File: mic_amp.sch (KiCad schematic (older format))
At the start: 12 parts

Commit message: * Sch edited and checked
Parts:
- removed C?: C, CAP_0603, symbol C
- removed R?: R, RES_0603, symbol R
- removed XL?: CONN_2, symbol CONN_2
- added C1: 10n, CAP_0603, symbol C
- added C2, C9: 1u, CAP_0603, symbol C
- added C6: 0.1u, CAP_0603, symbol C
- added DA1: NCP662SQ, symbol NCP662SQ
- added F1, F2, F3: Fuse0R, symbol Fuse0R
- added R1: 1M, RES_0603, symbol R
- added R5: 20k, symbol RVar
- added XL1: USB_MINI_B, symbol USB_MINI_B
- added XL2, XL3: CONN_AUDIO_SIMPLE, symbol CONN_AUDIO_SIMPLE
- R2: renamed from R?; value 2.21k -> 2k
- gave numbers to parts that had none: 8
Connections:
- net GND: now also D1.11 (NC), D1.4 (NC), C1.2, C2.2, C6.2, DA1.1 (GND), F1.2, F3.2, R1.2, R5.2, XL1.4 (UGND), XL1.5 (UID), XL2.1 (COM), XL2.H, XL3.1 (COM), XL3.H; no longer D1.9 (A/R)
- net MICBIAS: now also D1.13 (MICBIAS), R2.2, R3.1; no longer R3.2
- net VDD: now also C6.1, DA1.3 (Vout), F2.1; no longer D1.10 (GAIN)
- net at D1.14 (TH), R4.1: now also R3.2; no longer R3.1
- net at D1.6 (OUT): now also C9.1
- net MICIN: now reaches C4.2, D1.8 (MICIN)
- net at C4.1, R2.1: now also XL2.3 (L_IN)
- new net: D1.10 (GAIN), F2.2, F3.1
- new net: D1.9 (A/R), F1.1
- new net: R5.3, XL3.3 (L_IN)
- new net: C9.2, R5.1
- new net: C2.1, DA1.2 (Vin), DA1.4 (EN), XL1.1 (UVcc)
- new net: C1.1, R1.1, XL1.SHLD
- no-connect marks 0 -> 4
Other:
- note added: "Attack/release ratio:\nSoldered: 1:500\nNot soldered: 1:4000"
- note added: "Connect TH to MICBIAS\nto disable the AGC."
- note added: "Gain select:\nGAIN = Vdd: gain = 40dB\nGAIN = GND: gain = 50dB\nGAIN not connected: gain = 60dB"
- moved on the sheet: C4, R2, R3, R4

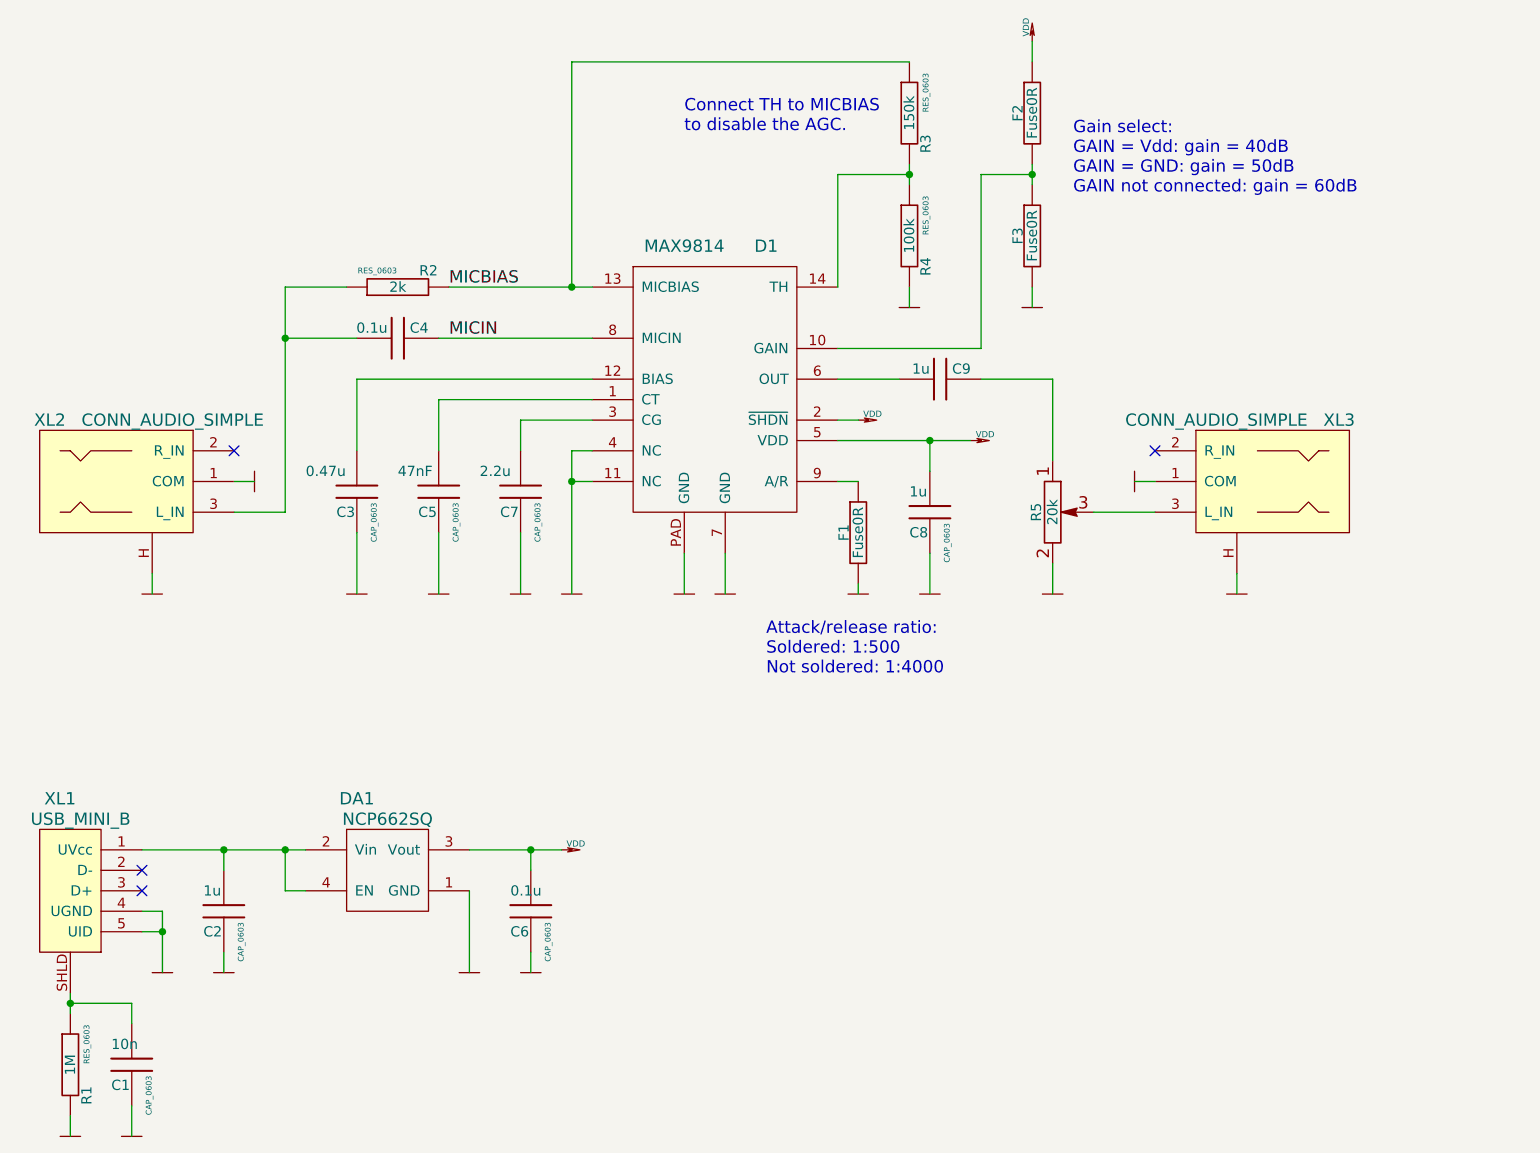
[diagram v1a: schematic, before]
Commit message: * Sch done + Components association
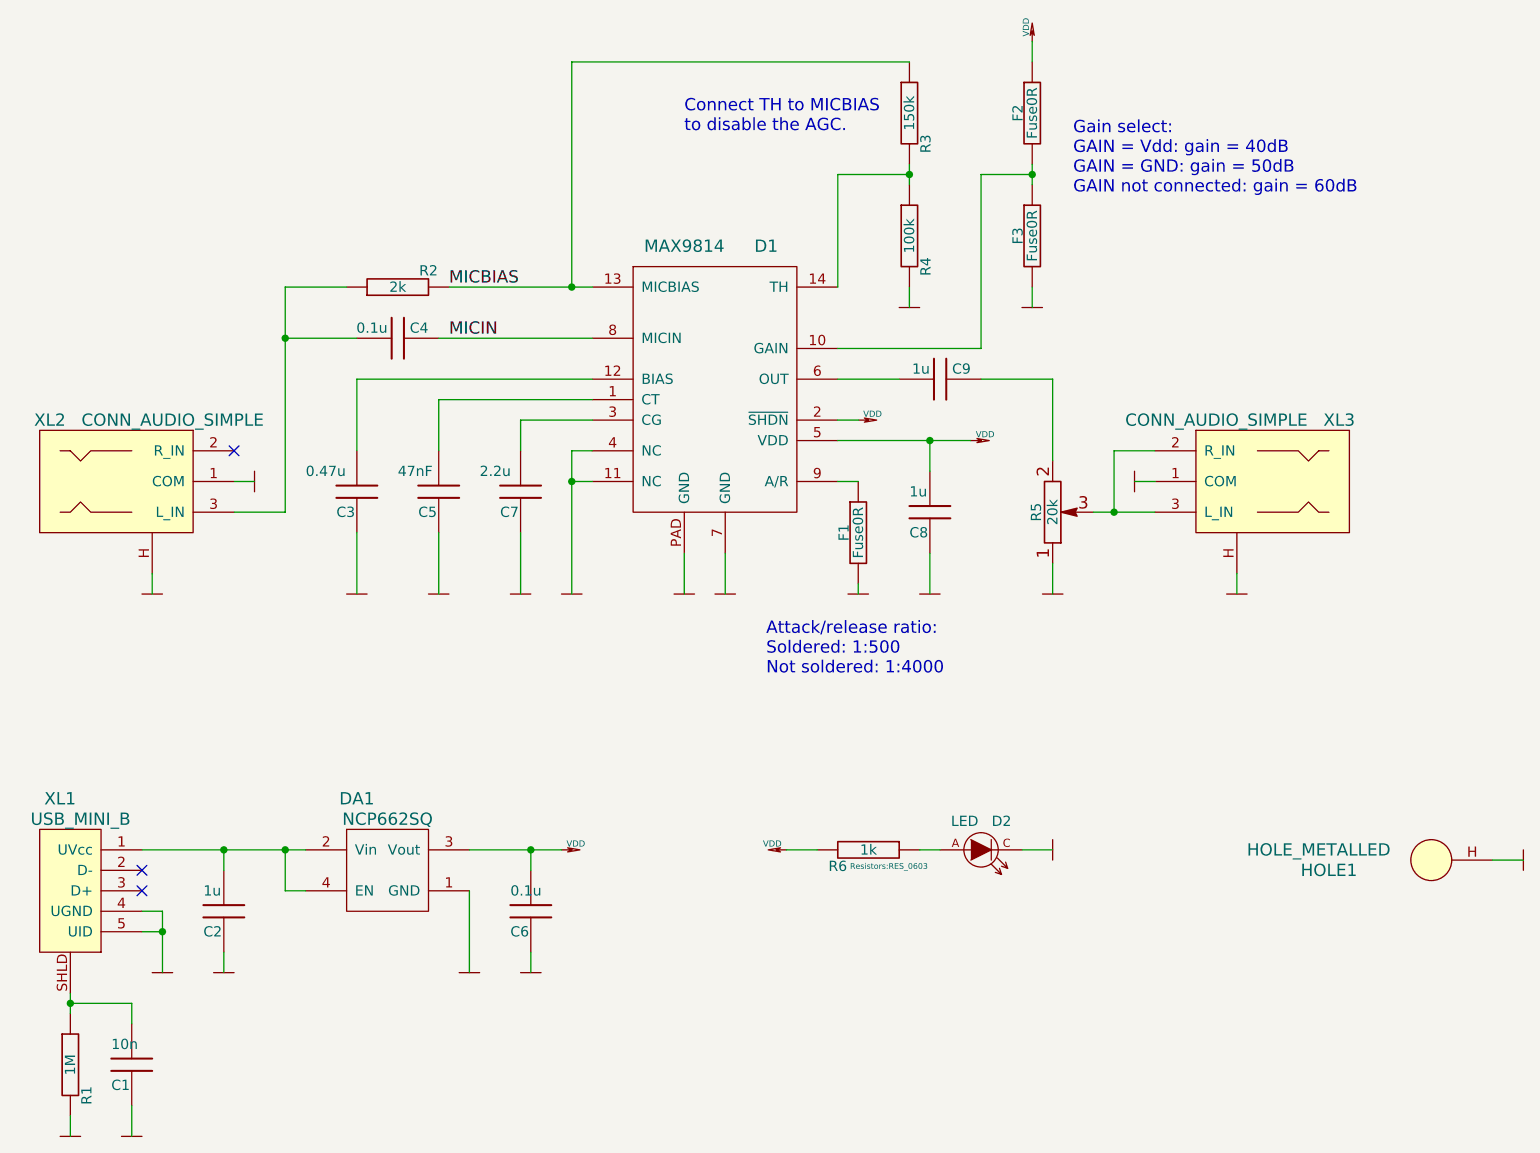
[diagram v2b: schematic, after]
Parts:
- added D2: LED, LEDs:LED_0603, symbol LED
- added HOLE1: HOLE_METALLED, PCB:Hole3_5_out6mm, symbol HOLE_METALLED
- added R6: 1k, Resistors:RES_0603, symbol R
- C1, C2, C3, C4, C5, C6, C7, C8, C9: footprint CAP_0603 -> Capacitors:CAP_0603
- D1: footprint (none) -> QFN_DFN:DFN14
- DA1: footprint (none) -> SOT:SC82AB
- F1, F2, F3: footprint (none) -> Resistors:RES_0603_SOLDERFUSE
- R1, R2, R3, R4: footprint RES_0603 -> Resistors:RES_0603
- R5: footprint (none) -> Resistors:VAR_PTV09A-4
- XL1: footprint (none) -> Connectors:USBmicro_MOLEX_WM17142
- XL2, XL3: footprint (none) -> Connectors:AUDIO_CKX3_5_30
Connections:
- net GND: now also R5.1, D2.C, HOLE1.H; no longer R5.2
- net VDD: now also R6.2
- net at XL3.2 (R_IN): now also R5.3, XL3.3 (L_IN)
- net at C9.2: now also R5.2; no longer R5.1
- new net: D2.A, R6.1
- no-connect marks 4 -> 3
